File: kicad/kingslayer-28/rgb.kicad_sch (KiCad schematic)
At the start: 29 parts, among them IC2 IS31FL3731-QFLS2-TR

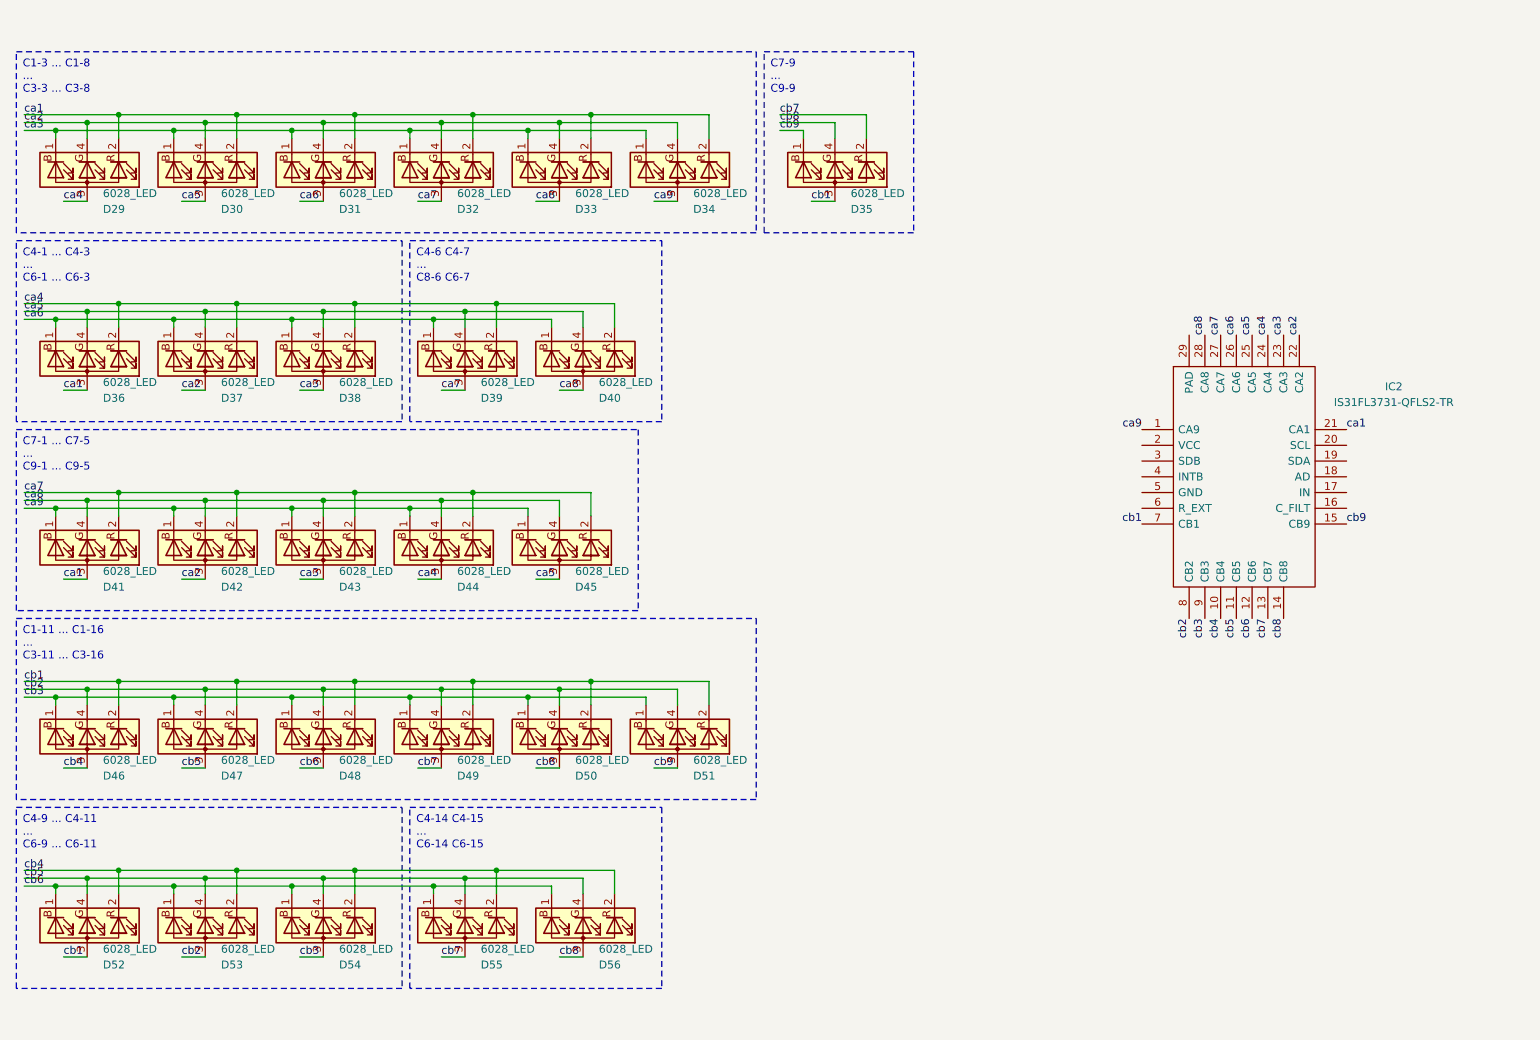
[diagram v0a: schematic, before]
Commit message: connect rgb
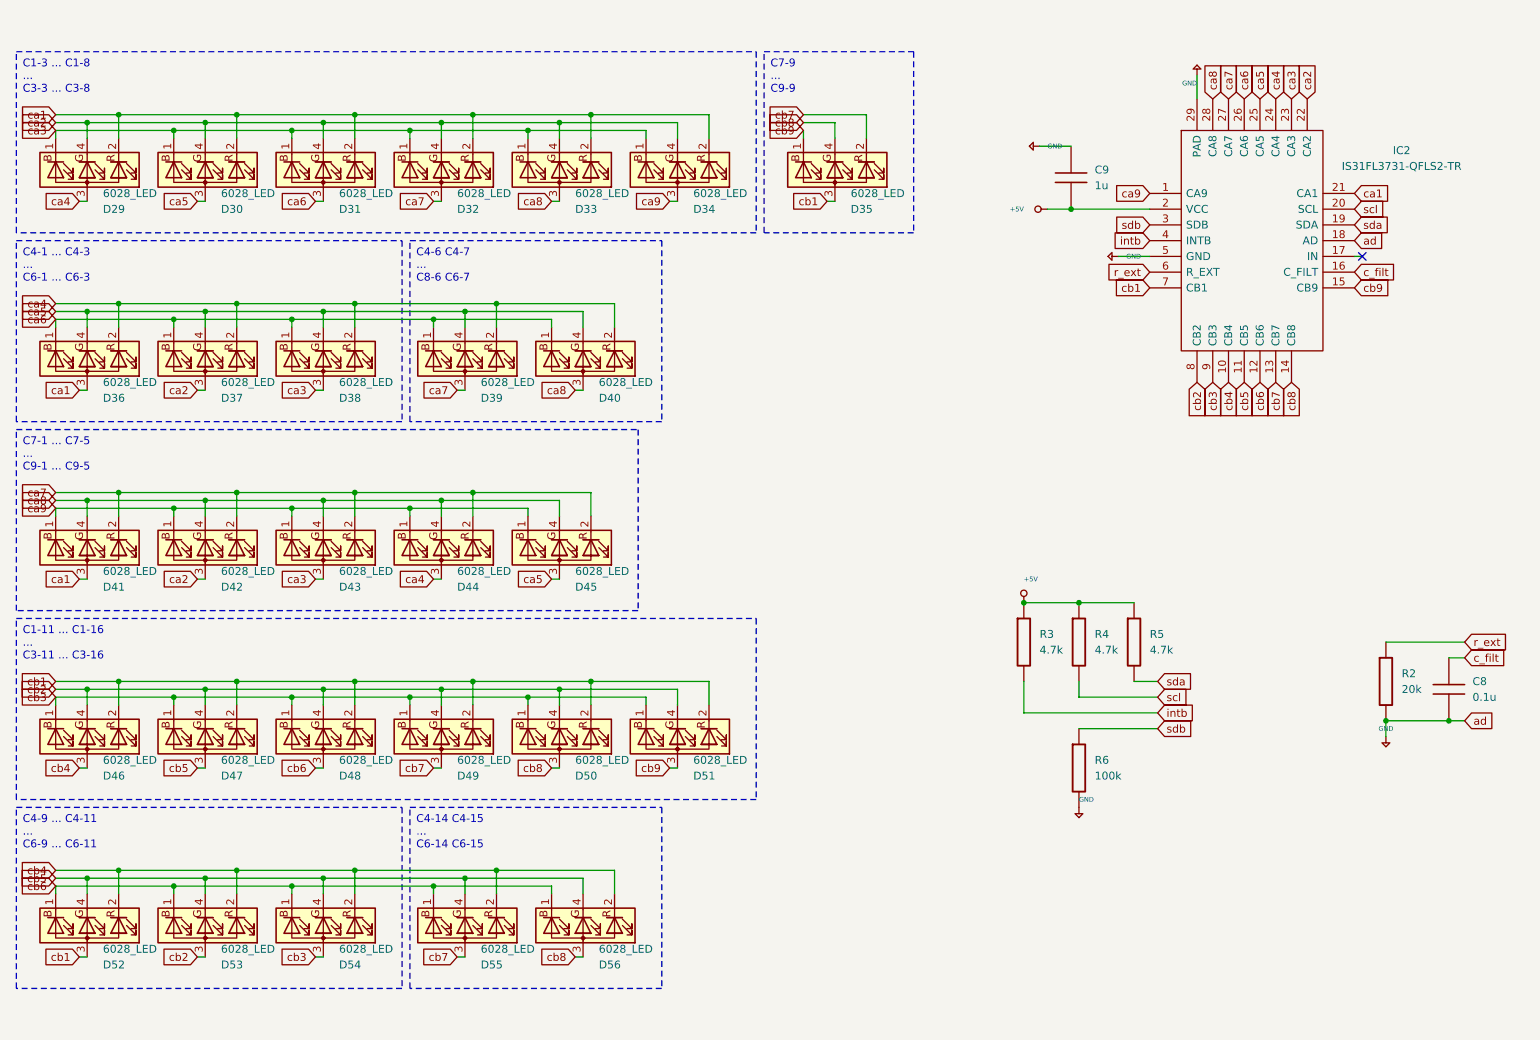
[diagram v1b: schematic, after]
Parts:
- added C8: 0.1u, symbol keyboard_parts:C
- added C9: 1u, symbol keyboard_parts:C
- added R2: 20k, symbol keyboard_parts:R
- added R3, R4, R5: 4.7k, symbol keyboard_parts:R
- added R6: 100k, symbol keyboard_parts:R
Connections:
- net c_filt: now reaches IC2.16 (C_FILT)
- net c_filt: now also C8.1
- net +5V: now reaches IC2.18 (AD)
- net +5V: now also IC2.2 (VCC), IC2.29 (PAD), IC2.5 (GND), C8.2, C9.1, C9.2, R2.2, R3.1, R4.1, R5.1, R6.2
- net sda: now reaches IC2.19 (SDA)
- net sda: now also R5.2
- net scl: now reaches IC2.20 (SCL)
- net scl: now also R4.2
- net sdb: now reaches IC2.3 (SDB)
- net sdb: now also R6.1
- net intb: now reaches IC2.4 (INTB)
- net intb: now also R3.2
- net r_ext: now reaches IC2.6 (R_EXT)
- net r_ext: now also R2.1
- no-connect marks 0 -> 1
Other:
- moved on the sheet: IC2

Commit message: add info
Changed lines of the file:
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@@
     (stroke (width 0) (type default))
   )
-  (wire (pts (xy 205.74 63.5) (xy 210.82 63.5))
+  (wire (pts (xy 209.55 63.5) (xy 210.82 63.5))
     (stroke (width 0) (type default))
   )
@@
       (effects (font (size 0.508 0.508)) hide)
     )
-    (property "Value" "GND" (at 199.3899 151.13 0)
+    (property "Value" "GND" (at 198.12 154.94 0)
       (effects (font (size 0.762 0.762)) (justify left))
     )
@@
   )
   (symbol (lib_id "keyboard_parts:GND") (at 248.92 140.97 0) (unit 1)
-    (in_bom yes) (on_board yes) (dnp no) (fields_autoplaced)
+    (in_bom yes) (on_board yes) (dnp no)
     (property "Reference" "#PWR015" (at 248.92 139.7 0)
       (effects (font (size 0.508 0.508)) hide)
     )
-    (property "Value" "GND" (at 248.92 139.7 0)
+    (property "Value" "GND" (at 248.92 143.51 0)
       (effects (font (size 0.762 0.762)))
     )
@@
       (effects (font (size 0.508 0.508)) hide)
     )
-    (property "Value" "GND" (at 218.4401 35.56 0)
+    (property "Value" "GND" (at 219.71 31.75 0)
       (effects (font (size 0.762 0.762)) (justify left))
     )
@@
     )
   )
-  (symbol (lib_id "keyboard_parts:GND") (at 205.74 63.5 270) (unit 1)
-    (in_bom yes) (on_board yes) (dnp no)
-    (property "Reference" "#PWR021" (at 207.01 63.5 0)
+  (symbol (lib_id "keyboard_parts:GND") (at 209.55 63.5 270) (unit 1)
+    (in_bom yes) (on_board yes) (dnp no)
+    (property "Reference" "#PWR021" (at 210.82 63.5 0)
       (effects (font (size 0.508 0.508)) hide)
     )
-    (property "Value" "GND" (at 207.01 63.4999 90)
+    (property "Value" "GND" (at 204.47 63.5 90)
       (effects (font (size 0.762 0.762)) (justify left))
     )
-    (property "Footprint" "" (at 205.74 63.5 0)
-      (effects (font (size 1.524 1.524)))
-    )
-    (property "Datasheet" "" (at 205.74 63.5 0)
+    (property "Footprint" "" (at 209.55 63.5 0)
+      (effects (font (size 1.524 1.524)))
+    )
+    (property "Datasheet" "" (at 209.55 63.5 0)
       (effects (font (size 1.524 1.524)))
     )
@@
       (effects (font (size 0.508 0.508)) hide)
     )
-    (property "Value" "GND" (at 194.31 45.7199 90)
+    (property "Value" "GND" (at 187.96 45.72 90)
       (effects (font (size 0.762 0.762)) (justify left))
     )

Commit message: Addressed some comments
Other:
- note added: "The I2C pins are 5v tolerant but I might want to change this to 3v3"
- moved on the sheet: D29, D30, D31, D32, D33, D34, D35, D36, D37, D38, D39, D40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

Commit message: update pics
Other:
- note added: "The I2C pins are 5v tolerant but it's still best to pull this up to 3v3"
- note removed: "The I2C pins are 5v tolerant but I might want to change this to 3v3"
- moved on the sheet: R6
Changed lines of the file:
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@@
   (junction (at 82.55 135.89) (diameter 0) (color 0 0 0 0)
   )
+  (junction (at 39.37 170.18) (diameter 0) (color 0 0 0 0)
+  )
+  (junction (at 58.42 71.12) (diameter 0) (color 0 0 0 0)
+  )
+  (junction (at 63.5 69.85) (diameter 0) (color 0 0 0 0)
+  )
+  (junction (at 82.55 69.85) (diameter 0) (color 0 0 0 0)
+  )
+  (junction (at 77.47 71.12) (diameter 0) (color 0 0 0 0)
+  )
+  (junction (at 95.25 171.45) (diameter 0) (color 0 0 0 0)
+  )
+  (junction (at 72.39 138.43) (diameter 0) (color 0 0 0 0)
+  )
+  (junction (at 110.49 39.37) (diameter 0) (color 0 0 0 0)
+  )
+  (junction (at 198.12 55.88) (diameter 0) (color 0 0 0 0)
+  )
+  (junction (at 96.52 38.1) (diameter 0) (color 0 0 0 0)
+  )
+  (junction (at 105.41 168.91) (diameter 0) (color 0 0 0 0)
+  )
+  (junction (at 53.34 72.39) (diameter 0) (color 0 0 0 0)
+  )
+  (junction (at 101.6 102.87) (diameter 0) (color 0 0 0 0)
+  )
+  (junction (at 39.37 71.12) (diameter 0) (color 0 0 0 0)
+  )
+  (junction (at 63.5 168.91) (diameter 0) (color 0 0 0 0)
+  )
+  (junction (at 77.47 137.16) (diameter 0) (color 0 0 0 0)
+  )
+  (junction (at 101.6 135.89) (diameter 0) (color 0 0 0 0)
+  )
+  (junction (at 58.42 137.16) (diameter 0) (color 0 0 0 0)
+  )
+  (junction (at 63.5 135.89) (diameter 0) (color 0 0 0 0)
+  )
+  (junction (at 72.39 171.45) (diameter 0) (color 0 0 0 0)
+  )
+  (junction (at 72.39 72.39) (diameter 0) (color 0 0 0 0)
+  )
   (junction (at 190.5 119.38) (diameter 0) (color 0 0 0 0)
-  )
-  (junction (at 39.37 170.18) (diameter 0) (color 0 0 0 0)
-  )
-  (junction (at 58.42 71.12) (diameter 0) (color 0 0 0 0)
-  )
-  (junction (at 63.5 69.85) (diameter 0) (color 0 0 0 0)
-  )
-  (junction (at 82.55 69.85) (diameter 0) (color 0 0 0 0)
-  )
-  (junction (at 77.47 71.12) (diameter 0) (color 0 0 0 0)
-  )
-  (junction (at 95.25 171.45) (diameter 0) (color 0 0 0 0)
-  )
-  (junction (at 72.39 138.43) (diameter 0) (color 0 0 0 0)
-  )
-  (junction (at 110.49 39.37) (diameter 0) (color 0 0 0 0)
-  )
-  (junction (at 198.12 55.88) (diameter 0) (color 0 0 0 0)
-  )
-  (junction (at 96.52 38.1) (diameter 0) (color 0 0 0 0)
-  )
-  (junction (at 105.41 168.91) (diameter 0) (color 0 0 0 0)
-  )
-  (junction (at 53.34 72.39) (diameter 0) (color 0 0 0 0)
-  )
-  (junction (at 101.6 102.87) (diameter 0) (color 0 0 0 0)
-  )
-  (junction (at 39.37 71.12) (diameter 0) (color 0 0 0 0)
-  )
-  (junction (at 63.5 168.91) (diameter 0) (color 0 0 0 0)
-  )
-  (junction (at 77.47 137.16) (diameter 0) (color 0 0 0 0)
-  )
-  (junction (at 101.6 135.89) (diameter 0) (color 0 0 0 0)
-  )
-  (junction (at 58.42 137.16) (diameter 0) (color 0 0 0 0)
-  )
-  (junction (at 63.5 135.89) (diameter 0) (color 0 0 0 0)
-  )
-  (junction (at 72.39 171.45) (diameter 0) (color 0 0 0 0)
-  )
-  (junction (at 72.39 72.39) (diameter 0) (color 0 0 0 0)
   )
   (junction (at 44.45 69.85) (diameter 0) (color 0 0 0 0)
@@
     (stroke (width 0) (type default))
   )
-  (wire (pts (xy 199.39 139.7) (xy 212.09 139.7))
+  (wire (pts (xy 190.5 139.7) (xy 212.09 139.7))
     (stroke (width 0) (type default))
   )
@@
     (effects (font (size 1.27 1.27)) (justify left top))
   )
-  (text "The I2C pins are 5v tolerant\nbut I might want to change this to 3v3"
+  (text "The I2C pins are 5v tolerant\nbut it's still best to pull this up to 3v3"
     (at 179.07 113.03 0)
     (effects (font (size 1.27 1.27)) (justify left bottom))
@@
     )
   )
-  (global_label "sda" (shape input) (at 243.84 58.42 0) (fields_autoplaced)
-    (effects (font (size 1.27 1.27)) (justify left))
-    (property "Intersheetrefs" "${INTERSHEET_REFS}" (at 250.1513 58.42 0)
-      (effects (font (size 1.27 1.27)) (justify left) hide)
-    )
-  )
   (global_label "ca9" (shape input) (at 210.82 53.34 180) (fields_autoplaced)
     (effects (font (size 1.27 1.27)) (justify right))
@@
     )
   )
-  (global_label "scl" (shape input) (at 212.09 134.62 0) (fields_autoplaced)
-    (effects (font (size 1.27 1.27)) (justify left))
-    (property "Intersheetrefs" "${INTERSHEET_REFS}" (at 217.8571 134.62 0)
-      (effects (font (size 1.27 1.27)) (justify left) hide)
-    )
-  )
   (global_label "cb3" (shape input) (at 220.98 83.82 270) (fields_autoplaced)
     (effects (font (size 1.27 1.27)) (justify right))
@@
     )
   )
-  (global_label "sda" (shape input) (at 212.09 132.08 0) (fields_autoplaced)
-    (effects (font (size 1.27 1.27)) (justify left))
-    (property "Intersheetrefs" "${INTERSHEET_REFS}" (at 218.4013 132.08 0)
-      (effects (font (size 1.27 1.27)) (justify left) hide)
-    )
-  )
   (global_label "ca8" (shape input) (at 220.98 38.1 90) (fields_autoplaced)
     (effects (font (size 1.27 1.27)) (justify left))
@@
     )
   )
-  (global_label "scl" (shape input) (at 243.84 55.88 0) (fields_autoplaced)
+  (global_label "ca4" (shape input) (at 38.1 50.8 180) (fields_autoplaced)
+    (effects (font (size 1.27 1.27)) (justify right))
+    (property "Intersheetrefs" "${INTERSHEET_REFS}" (at 31.6677 50.8 0)
+      (effects (font (size 1.27 1.27)) (justify right) hide)
+    )
+  )
+  (hierarchical_label "scl" (shape bidirectional) (at 212.09 134.62 0) (fields_autoplaced)
     (effects (font (size 1.27 1.27)) (justify left))
-    (property "Intersheetrefs" "${INTERSHEET_REFS}" (at 249.6071 55.88 0)
-      (effects (font (size 1.27 1.27)) (justify left) hide)
-    )
-  )
-  (global_label "ca4" (shape input) (at 38.1 50.8 180) (fields_autoplaced)
-    (effects (font (size 1.27 1.27)) (justify right))
-    (property "Intersheetrefs" "${INTERSHEET_REFS}" (at 31.6677 50.8 0)
-      (effects (font (size 1.27 1.27)) (justify right) hide)
-    )
+  )
+  (hierarchical_label "scl" (shape bidirectional) (at 243.84 55.88 0) (fields_autoplaced)
+    (effects (font (size 1.27 1.27)) (justify left))
+  )
+  (hierarchical_label "sda" (shape bidirectional) (at 243.84 58.42 0) (fields_autoplaced)
+    (effects (font (size 1.27 1.27)) (justify left))
+  )
+  (hierarchical_label "sda" (shape bidirectional) (at 212.09 132.08 0) (fields_autoplaced)
+    (effects (font (size 1.27 1.27)) (justify left))
   )
   (symbol (lib_id "Device:LED_BRAG") (at 77.47 78.74 270) (unit 1)
@@
         (path "/7c3679ab-fb1a-4578-bd30-c0b9ef7b8f3d/1d89b5f7-42e5-454c-b5cc-40443ecfd48e"
           (reference "D36") (unit 1)
+        )
+      )
+    )
+  )
+  (symbol (lib_id "keyboard_parts:+3V3") (at 190.5 119.38 0) (unit 1)
+    (in_bom yes) (on_board yes) (dnp no) (fields_autoplaced)
+    (property "Reference" "#PWR018" (at 190.5 120.142 0)
+      (effects (font (size 0.508 0.508)) hide)
+    )
+    (property "Value" "+3V3" (at 190.5 115.57 0)
+      (effects (font (size 0.762 0.762)))
+    )
+    (property "Footprint" "" (at 190.5 119.38 0)
+      (effects (font (size 1.524 1.524)))
+    )
+    (property "Datasheet" "" (at 190.5 119.38 0)
+      (effects (font (size 1.524 1.524)))
+    )
+    (pin "1")
+    (instances
+      (project "kingslayer-28"
+        (path "/7c3679ab-fb1a-4578-bd30-c0b9ef7b8f3d/1d89b5f7-42e5-454c-b5cc-40443ecfd48e"
+          (reference "#PWR018") (unit 1)
         )
       )
@@
     )
   )
-  (symbol (lib_id "keyboard_parts:R") (at 199.39 146.05 0) (unit 1)
+  (symbol (lib_id "keyboard_parts:R") (at 190.5 146.05 0) (unit 1)
     (in_bom yes) (on_board yes) (dnp no) (fields_autoplaced)
-    (property "Reference" "R6" (at 201.93 144.78 0)
-      (effects (font (size 1.27 1.27)) (justify left))
-    )
-    (property "Value" "100k" (at 201.93 147.32 0)
-      (effects (font (size 1.27 1.27)) (justify left))
-    )
-    (property "Footprint" "" (at 199.39 146.05 0)
-      (effects (font (size 1.524 1.524)))
-    )
-    (property "Datasheet" "~" (at 199.39 146.05 0)
+    (property "Reference" "R6" (at 193.04 144.78 0)
+      (effects (font (size 1.27 1.27)) (justify left))
+    )
+    (property "Value" "100k" (at 193.04 147.32 0)
+      (effects (font (size 1.27 1.27)) (justify left))
+    )
+    (property "Footprint" "" (at 190.5 146.05 0)
+      (effects (font (size 1.524 1.524)))
+    )
+    (property "Datasheet" "~" (at 190.5 146.05 0)
       (effects (font (size 1.524 1.524)))
     )
@@
     )
   )
-  (symbol (lib_id "keyboard_parts:GND") (at 199.39 152.4 0) (unit 1)
-    (in_bom yes) (on_board yes) (dnp no)
-    (property "Reference" "#PWR019" (at 199.39 151.13 0)
+  (symbol (lib_id "keyboard_parts:GND") (at 190.5 152.4 0) (unit 1)
+    (in_bom yes) (on_board yes) (dnp no)
+    (property "Reference" "#PWR019" (at 190.5 151.13 0)
       (effects (font (size 0.508 0.508)) hide)
     )
-    (property "Value" "GND" (at 198.12 154.94 0)
+    (property "Value" "GND" (at 189.23 154.94 0)
       (effects (font (size 0.762 0.762)) (justify left))
     )
-    (property "Footprint" "" (at 199.39 152.4 0)
-      (effects (font (size 1.524 1.524)))
-    )
-    (property "Datasheet" "" (at 199.39 152.4 0)
+    (property "Footprint" "" (at 190.5 152.4 0)
+      (effects (font (size 1.524 1.524)))
+    )
+    (property "Datasheet" "" (at 190.5 152.4 0)
       (effects (font (size 1.524 1.524)))
     )
@@
         )
       )
-    )
-  )
-  (symbol (lib_id "keyboard_parts:+5V") (at 190.5 119.38 0) (unit 1)
-    (in_bom yes) (on_board yes) (dnp no)
-    (property "Reference" "#PWR018" (at 190.5 120.142 0)
-      (effects (font (size 0.508 0.508)) hide)
-    )
-    (property "Value" "+5V" (at 190.5001 115.57 0)
-      (effects (font (size 0.762 0.762)) (justify left))
-    )
-    (property "Footprint" "" (at 190.5 119.38 0)
-      (effects (font (size 1.524 1.524)))
-    )
-    (property "Datasheet" "" (at 190.5 119.38 0)
-      (effects (font (size 1.524 1.524)))
-    )
-    (pin "1")
-    (instances
-      (project "kingslayer-28"
-        (path "/7c3679ab-fb1a-4578-bd30-c0b9ef7b8f3d/1d89b5f7-42e5-454c-b5cc-40443ecfd48e"
-          (reference "#PWR018") (unit 1)
-        )
-      )
